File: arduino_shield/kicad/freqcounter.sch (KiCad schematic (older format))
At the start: 29 parts, among them J1 ICSP PICKIT, J10 INPUT_A, J11 INPUT_B, J12 INPUT_ZCD, J13 I2C_1, J14 I2C_2, J15 PARALEL, J2 Arduino_Power, J3 Arduino_Power, J4 Arduino_Digital_2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

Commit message: Arduino Shield PCB designed
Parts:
- removed J5: Digital_2, Footprints:Connector_1x06, symbol Connector:Conn_01x06_Female
- removed J6: Analog, Footprints:Connector_1x04, symbol Connector:Conn_01x04_Female
- removed J8: Digital_1, Footprints:Connector_1x06, symbol Connector:Conn_01x06_Female
- added J5: Digital_2, Footprints:Connector_1x08, symbol Connector:Conn_01x08_Female
- added J6: Analog, Footprints:Connector_1x06, symbol Connector:Conn_01x06_Female
- added J8: Digital_1, Footprints:Connector_1x08, symbol Connector:Conn_01x08_Female
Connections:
- net VDD is gone; now on net 5V: J1.2 (Pin_2), J13.3 (Pin_3), J14.3 (Pin_3), J15.1 (Pin_1), R5.1, R6.1
- net ARD_RX: now also U1.11 (RB6), J8.8 (Pin_8); no longer U1.15 (RC1)
- net ARD_TX: now also J8.7 (Pin_7)
- net GND: now also J5.2 (Pin_2)
- net P0: now also U1.13 (RB4); no longer U1.9 (RC7)
- net P1: now also U1.14 (RC2); no longer U1.10 (RB7)
- net P2: now also U1.15 (RC1); no longer U1.11 (RB6)
- net P3: now also U1.16 (RC0); no longer U1.12 (RB5)
- net SCL: now also U1.10 (RB7), J6.6 (Pin_6); no longer U1.13 (RB4)
- net SDA: now also U1.9 (RC7), J6.5 (Pin_5); no longer U1.14 (RC2)
- net at J4.1 (Pin_1): now also J5.1 (Pin_1)
- net at J4.3 (Pin_3): now also J5.3 (Pin_3)
- net at J4.4 (Pin_4): now also J5.4 (Pin_4)
- net at J4.5 (Pin_5): now also J5.5 (Pin_5)
- net at J4.6 (Pin_6): now also J5.6 (Pin_6)
- net at J4.7 (Pin_7): now also J5.7 (Pin_7)
- net at J4.8 (Pin_8): now also J5.8 (Pin_8)
- net at J9.1 (Pin_1): now also J8.1 (Pin_1)
- net at J9.2 (Pin_2): now also J8.2 (Pin_2)
- net at J9.3 (Pin_3): now also J8.3 (Pin_3)
- net at J9.4 (Pin_4): now also J8.4 (Pin_4)
- net at J9.5 (Pin_5): now also J8.5 (Pin_5)
- net at J9.6 (Pin_6): now also J8.6 (Pin_6)
- net at J7.1 (Pin_1): now also J6.1 (Pin_1)
- net at J7.2 (Pin_2): now also J6.2 (Pin_2)
- net at J7.3 (Pin_3): now also J6.3 (Pin_3)
- net at J7.4 (Pin_4): now also J6.4 (Pin_4)
- net at R2.2: now also U1.12 (RB5); no longer U1.16 (RC0)
- no-connect marks 2 -> 1
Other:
- moved on the sheet: R2
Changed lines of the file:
@@
 MCLR
 Text GLabel 6700 1000 0    40   Input ~ 0
-VDD
+5V
 Text GLabel 6700 1100 0    40   Input ~ 0
 GND
@@
 P 2900 1500
 F 0 "J4" H 2800 1500 50  0000 C CNN
-F 1 "Arduino_Digital_2" H 3000 1950 50  0000 C CNN
+F 1 "Arduino_Digital_2" H 2800 1950 50  0000 C CNN
 F 2 "Footprints:Connector_1x08" H 2900 1500 50  0001 C CNN
 F 3 "~" H 2900 1500 50  0001 C CNN
@@
 Text Notes 1200 900  0    100  ~ 0
 ARDUINO INTERFACE
-Text GLabel 1200 2700 2    40   Input ~ 0
+Text GLabel 1400 2900 2    40   Input ~ 0
 SCL
-Text GLabel 1200 2600 2    40   Input ~ 0
+Text GLabel 1400 2800 2    40   Input ~ 0
 SDA
-Text GLabel 2700 2900 0    40   Input ~ 0
+Text GLabel 2500 3100 0    40   Input ~ 0
 ARD_RX
-Text GLabel 2700 2800 0    40   Input ~ 0
+Text GLabel 2500 3000 0    40   Input ~ 0
 ARD_TX
 Text GLabel 1200 1600 2    40   Input ~ 0
@@
 Text GLabel 1200 1300 2    40   Input ~ 0
 3.3V
-Text GLabel 2700 1300 0    40   Input ~ 0
-GND
-Text GLabel 8000 2800 2    40   Input ~ 0
+Text GLabel 8000 3200 2    40   Input ~ 0
 ARD_TX
-Text GLabel 7200 2900 2    40   Input ~ 0
+Text GLabel 7200 3300 2    40   Input ~ 0
 ARD_RX
-Text GLabel 7200 3100 2    40   Input ~ 0
+Text GLabel 6200 3300 0    40   Input ~ 0
 SCL
-Text GLabel 7200 3000 2    40   Input ~ 0
+Text GLabel 6200 3200 0    40   Input ~ 0
 SDA
 $Comp
@@
 L Device:R R2
 U 1 1 5EA58FDB
-P 7650 2800
-F 0 "R2" V 7600 2950 50  0000 L CNN
-F 1 "180" V 7645 2725 50  0000 L CNN
-F 2 "Resistor_SMD:R_0805_2012Metric_Pad1.15x1.40mm_HandSolder" V 7580 2800 50  0001 C CNN
-F 3 "~" H 7650 2800 50  0001 C CNN
-	1    7650 2800
+P 7650 3200
+F 0 "R2" V 7600 3350 50  0000 L CNN
+F 1 "180" V 7645 3125 50  0000 L CNN
+F 2 "Resistor_SMD:R_0805_2012Metric_Pad1.15x1.40mm_HandSolder" V 7580 3200 50  0001 C CNN
+F 3 "~" H 7650 3200 50  0001 C CNN
+	1    7650 3200
 	0    1    1    0
 $EndComp
 Wire Wire Line
-	8000 2800 7800 2800
-Wire Wire Line
-	7500 2800 7200 2800
+	8000 3200 7800 3200
+Wire Wire Line
+	7500 3200 7200 3200
 $Comp
 L Device:C C1
@@
 $EndComp
 Text GLabel 7700 5100 2    40   Input ~ 0
-VDD
+5V
 Wire Wire Line
 	7700 4900 7600 4900
@@
 $EndComp
 Text GLabel 8400 5100 2    40   Input ~ 0
-VDD
+5V
 Wire Wire Line
 	8400 4900 8300 4900
@@
 Text GLabel 8400 5000 2    40   Input ~ 0
 SDA
-Text GLabel 7200 3200 2    40   Input ~ 0
+Text GLabel 7200 2800 2    40   Input ~ 0
 P3
-Text GLabel 7200 3300 2    40   Input ~ 0
+Text GLabel 7200 2900 2    40   Input ~ 0
 P2
-Text GLabel 6200 3200 0    40   Input ~ 0
+Text GLabel 7200 3100 2    40   Input ~ 0
 P0
-Text GLabel 6200 3300 0    40   Input ~ 0
+Text GLabel 7200 3000 2    40   Input ~ 0
 P1
 Text GLabel 9100 5200 2    40   Input ~ 0
@@
 GND
 Text GLabel 9100 4900 2    40   Input ~ 0
-VDD
+5V
 Wire Wire Line
 	9100 4900 9000 4900
@@
 Text GLabel 6100 2400 0    40   Input ~ 0
 5V
-$Comp
-L Connector:Conn_01x06_Female J8
-U 1 1 5EA891A7
-P 2400 2400
-F 0 "J8" H 2500 2400 50  0000 C CNN
-F 1 "Digital_1" H 2350 2750 50  0000 C CNN
-F 2 "Footprints:Connector_1x06" H 2400 2400 50  0001 C CNN
-F 3 "~" H 2400 2400 50  0001 C CNN
-	1    2400 2400
-	-1   0    0    -1
-$EndComp
-$Comp
-L Connector:Conn_01x04_Female J6
-U 1 1 5EA9244B
-P 1500 2300
-F 0 "J6" H 1528 2275 50  0000 L CNN
-F 1 "Analog" H 1350 2550 50  0000 L CNN
-F 2 "Footprints:Connector_1x04" H 1500 2300 50  0001 C CNN
-F 3 "~" H 1500 2300 50  0001 C CNN
-	1    1500 2300
-	1    0    0    -1
-$EndComp
-Wire Wire Line
-	1200 2200 1300 2200
-Wire Wire Line
-	1300 2300 1200 2300
-Wire Wire Line
-	1200 2400 1300 2400
-Wire Wire Line
-	1300 2500 1200 2500
-Wire Wire Line
-	2600 2200 2700 2200
-Wire Wire Line
-	2700 2300 2600 2300
-Wire Wire Line
-	2600 2400 2700 2400
-Wire Wire Line
-	2700 2500 2600 2500
-Wire Wire Line
-	2600 2600 2700 2600
-Wire Wire Line
-	2700 2700 2600 2700
-NoConn ~ 2700 1200
-$Comp
-L Connector:Conn_01x06_Female J5
-U 1 1 5EAA5BE8
-P 2400 1600
-F 0 "J5" H 2500 1400 50  0000 C CNN
-F 1 "Digital_2" V 2500 1700 50  0000 C CNN
-F 2 "Footprints:Connector_1x06" H 2400 1600 50  0001 C CNN
-F 3 "~" H 2400 1600 50  0001 C CNN
-	1    2400 1600
-	-1   0    0    -1
-$EndComp
-Wire Wire Line
-	2600 1400 2700 1400
-Wire Wire Line
-	2700 1500 2600 1500
-Wire Wire Line
-	2600 1600 2700 1600
-Wire Wire Line
-	2700 1700 2600 1700
-Wire Wire Line
-	2600 1800 2700 1800
-Wire Wire Line
-	2700 1900 2600 1900
 Text GLabel 1200 1200 2    40   Input ~ 0
 Reset
@@
 Vin
 Wire Notes Line
-	600  3100 3500 3100
-Wire Notes Line
-	3500 3100 3500 600
-Wire Notes Line
 	3500 600  600  600
-Wire Notes Line
-	600  3100 600  600
 Text GLabel 8800 4100 3    40   Input ~ 0
 SCL
@@
 $EndComp
 Text GLabel 8800 3600 1    40   Input ~ 0
-VDD
+5V
 Wire Wire Line
 	8800 3600 8800 3650
@@
 Wire Wire Line
 	8800 3650 8800 3800
+$Comp
+L Connector:Conn_01x06_Female J6
+U 1 1 5EAB060A
+P 1600 2400
+F 0 "J6" H 1628 2375 50  0000 L CNN
+F 1 "Analog" H 1400 2750 50  0000 L CNN
+F 2 "Footprints:Connector_1x06" H 1600 2400 50  0001 C CNN
+F 3 "~" H 1600 2400 50  0001 C CNN
+	1    1600 2400
+	1    0    0    -1
+$EndComp
+Wire Wire Line
+	1200 2200 1400 2200
+Wire Wire Line
+	1200 2300 1400 2300
+Wire Wire Line
+	1200 2400 1400 2400
+Wire Wire Line
+	1200 2500 1400 2500
+Wire Wire Line
+	1200 2600 1300 2600
+Wire Wire Line
+	1200 2700 1400 2700
+Wire Wire Line
+	1200 2700 1200 2900
+Wire Wire Line
+	1200 2900 1400 2900
+Connection ~ 1200 2700
+Wire Wire Line
+	1400 2800 1300 2800
+Wire Wire Line
+	1300 2800 1300 2600
+Connection ~ 1300 2600
+Wire Wire Line
+	1300 2600 1400 2600
+Wire Wire Line
+	2500 3100 2700 3100
+Wire Wire Line
+	2700 3100 2700 2900
+Wire Wire Line
+	2500 3000 2600 3000
+Wire Wire Line
+	2600 3000 2600 2800
+Wire Wire Line
+	2600 2800 2700 2800
+$Comp
+L Connector:Conn_01x08_Female J8
+U 1 1 5EACC1E4
+P 2300 2500
+F 0 "J8" H 2328 2475 50  0000 L CNN
+F 1 "Digital_1" H 2100 2950 50  0000 L CNN
+F 2 "Footprints:Connector_1x08" H 2300 2500 50  0001 C CNN
+F 3 "~" H 2300 2500 50  0001 C CNN
+	1    2300 2500
+	-1   0    0    -1
+$EndComp
+Wire Wire Line
+	2500 2900 2700 2900
+Connection ~ 2700 2900
+Wire Wire Line
+	2600 2800 2500 2800
+Connection ~ 2600 2800
+Wire Wire Line
+	2500 2700 2700 2700
+Wire Wire Line
+	2500 2600 2700 2600
+Wire Wire Line
+	2500 2500 2700 2500
+Wire Wire Line
+	2500 2400 2700 2400
+Wire Wire Line
+	2500 2300 2700 2300
+Wire Wire Line
+	2500 2200 2700 2200
+Wire Notes Line
+	600  600  600  3300
+Wire Notes Line
+	600  3300 3500 3300
+Wire Notes Line
+	3500 3300 3500 600
+$Comp
+L Connector:Conn_01x08_Female J5
+U 1 1 5EAEC8C6
+P 2300 1500
+F 0 "J5" H 2328 1475 50  0000 L CNN
+F 1 "Digital_2" H 2100 1950 50  0000 L CNN
+F 2 "Footprints:Connector_1x08" H 2300 1500 50  0001 C CNN
+F 3 "~" H 2300 1500 50  0001 C CNN
+	1    2300 1500
+	-1   0    0    -1
+$EndComp
+Wire Wire Line
+	2500 1400 2700 1400
+Wire Wire Line
+	2500 1500 2700 1500
+Wire Wire Line
+	2500 1600 2700 1600
+Wire Wire Line
+	2500 1700 2700 1700
+Wire Wire Line
+	2500 1800 2700 1800
+Wire Wire Line
+	2500 1900 2700 1900
+Wire Wire Line
+	2700 1200 2500 1200
+Wire Wire Line
+	2700 1300 2600 1300
+Text GLabel 2250 1250 0    40   Input ~ 0
+GND
+Wire Wire Line
+	2250 1250 2600 1250
+Wire Wire Line
+	2600 1250 2600 1300
+Connection ~ 2600 1300
+Wire Wire Line
+	2600 1300 2500 1300
 $EndSCHEMATC

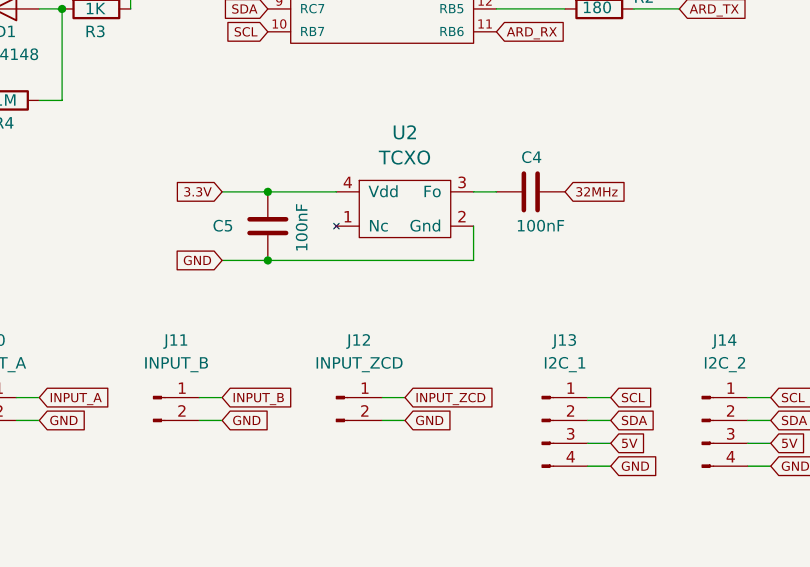
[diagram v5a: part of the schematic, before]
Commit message: Bugfix Arduino-Shield PCB
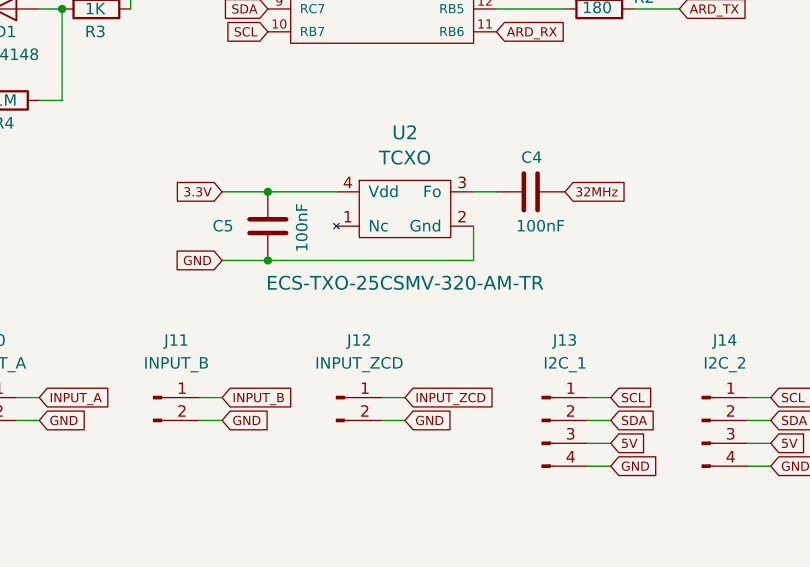
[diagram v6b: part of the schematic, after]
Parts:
- D1: footprint Diode_SMD:D_SOD-123 -> Footprints:SOD-80_HandSolder
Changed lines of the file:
@@
 F 0 "D1" H 5100 3100 50  0000 R CNN
 F 1 "1N4148" H 5200 3000 50  0000 R CNN
-F 2 "Diode_SMD:D_SOD-123" H 5050 3025 50  0001 C CNN
+F 2 "Footprints:SOD-80_HandSolder" H 5050 3025 50  0001 C CNN
 F 3 "https://www.vishay.com/docs/85748/1n4148w.pdf" H 5050 3200 50  0001 C CNN
 	1    5050 3200
@@
 F 1 "TCXO" H 6800 4148 60  0000 C CNN
 F 2 "Footprints:TCXO-5032" H 6700 3950 60  0001 C CNN
-F 3 "" H 6700 3950 60  0000 C CNN
+F 3 "ECS-TXO-25CSMV-320-AM-TR" H 6800 3600 60  0000 C CNN
 	1    6500 4000
 	1    0    0    -1

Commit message: Bugfix Arduino-Shield Schematic and PCB
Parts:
- added R7, R8, R9: 180, Resistor_SMD:R_0805_2012Metric_Pad1.15x1.40mm_HandSolder, symbol Device:R
- R5, R6: value 10K -> 2K2
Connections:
- net Earth is gone; now on net GND: C3.2
- net ARD_RX: now also R7.1; no longer U1.11 (RB6)
- net INPUT_A: now also R8.2; no longer U1.5 (RC5)
- net INPUT_B: now also R9.2; no longer U1.6 (RC4)
- new net: R7.2, U1.11 (RB6)
- new net: R8.1, U1.5 (RC5)
- new net: R9.1, U1.6 (RC4)
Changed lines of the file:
@@
-	0    1    -1   0
-$EndComp
-$Comp
-L power:Earth #PWR01
-U 1 1 5E71FD1E
-P 4400 3200
-F 0 "#PWR01" H 4400 2950 50  0001 C CNN
-F 1 "Earth" H 4400 3050 50  0001 C CNN
-F 2 "" H 4400 3200 50  0001 C CNN
-F 3 "~" H 4400 3200 50  0001 C CNN
-	1    4400 3200
 	0    1    -1   0
 $EndComp
@@
 Text GLabel 6700 1100 0    40   Input ~ 0
 GND
-Text GLabel 6200 2800 0    40   Input ~ 0
+Text GLabel 5500 2800 0    40   Input ~ 0
 INPUT_A
-Text GLabel 6200 2900 0    40   Input ~ 0
+Text GLabel 5500 2900 0    40   Input ~ 0
 INPUT_B
 $Comp
@@
 Text GLabel 8000 3200 2    40   Input ~ 0
 ARD_TX
-Text GLabel 7200 3300 2    40   Input ~ 0
+Text GLabel 8000 3300 2    40   Input ~ 0
 ARD_RX
 Text GLabel 6200 3300 0    40   Input ~ 0
@@
 P 8800 3950
 F 0 "R5" V 8750 4100 50  0000 L CNN
-F 1 "10K" V 8795 3875 50  0000 L CNN
+F 1 "2K2" V 8795 3875 50  0000 L CNN
 F 2 "Resistor_SMD:R_0805_2012Metric_Pad1.15x1.40mm_HandSolder" V 8730 3950 50  0001 C CNN
 F 3 "~" H 8800 3950 50  0001 C CNN
@@
 P 8900 3950
 F 0 "R6" V 8850 4100 50  0000 L CNN
-F 1 "10K" V 8895 3875 50  0000 L CNN
+F 1 "2K2" V 8895 3875 50  0000 L CNN
 F 2 "Resistor_SMD:R_0805_2012Metric_Pad1.15x1.40mm_HandSolder" V 8830 3950 50  0001 C CNN
 F 3 "~" H 8900 3950 50  0001 C CNN
@@
 Wire Wire Line
 	2600 1300 2500 1300
+$Comp
+L Device:R R8
+U 1 1 5EABD611
+P 5650 2800
+F 0 "R8" V 5600 2950 50  0000 L CNN
+F 1 "180" V 5645 2725 50  0000 L CNN
+F 2 "Resistor_SMD:R_0805_2012Metric_Pad1.15x1.40mm_HandSolder" V 5580 2800 50  0001 C CNN
+F 3 "~" H 5650 2800 50  0001 C CNN
+	1    5650 2800
+	0    1    1    0
+$EndComp
+$Comp
+L Device:R R9
+U 1 1 5EABD6A7
+P 5650 2900
+F 0 "R9" V 5600 3050 50  0000 L CNN
+F 1 "180" V 5645 2825 50  0000 L CNN
+F 2 "Resistor_SMD:R_0805_2012Metric_Pad1.15x1.40mm_HandSolder" V 5580 2900 50  0001 C CNN
+F 3 "~" H 5650 2900 50  0001 C CNN
+	1    5650 2900
+	0    1    1    0
+$EndComp
+Wire Wire Line
+	5800 2800 6200 2800
+Wire Wire Line
+	5800 2900 6200 2900
+$Comp
+L Device:R R7
+U 1 1 5EAC87AA
+P 7650 3300
+F 0 "R7" V 7600 3450 50  0000 L CNN
+F 1 "180" V 7645 3225 50  0000 L CNN
+F 2 "Resistor_SMD:R_0805_2012Metric_Pad1.15x1.40mm_HandSolder" V 7580 3300 50  0001 C CNN
+F 3 "~" H 7650 3300 50  0001 C CNN
+	1    7650 3300
+	0    1    1    0
+$EndComp
+Wire Wire Line
+	7800 3300 8000 3300
+Wire Wire Line
+	7500 3300 7200 3300
+Text GLabel 4400 3200 0    40   Input ~ 0
+GND
 $EndSCHEMATC

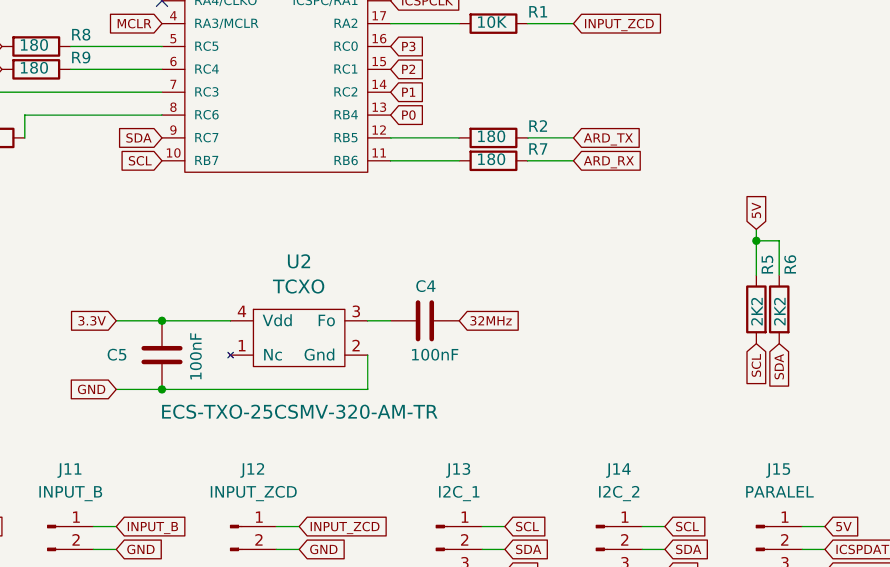
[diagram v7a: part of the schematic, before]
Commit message: Updated Arduino-Shield Schematic and PCB
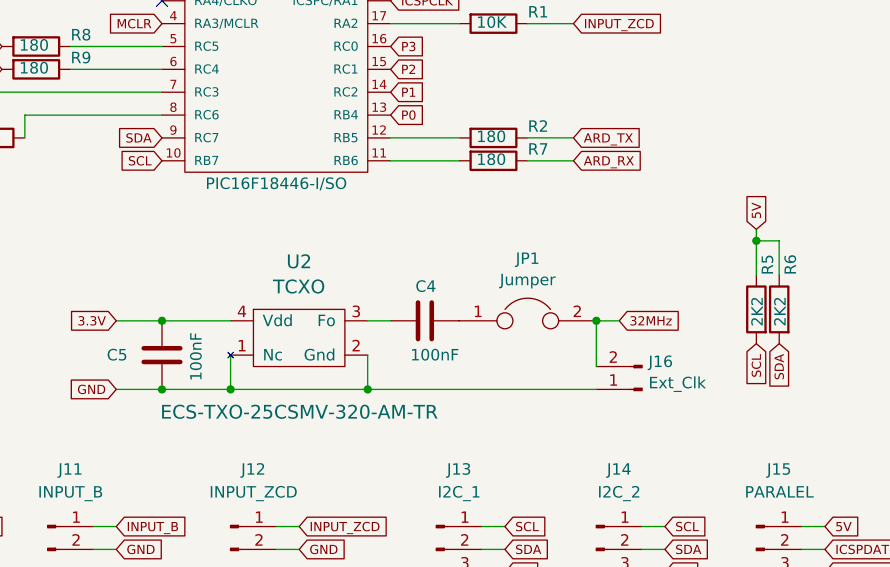
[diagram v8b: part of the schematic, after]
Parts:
- added J16: Ext_Clk, Footprints:PinHeader_1x02, symbol Connector:Conn_01x02_Male
- added JP1: Jumper, Footprints:PinHeader_1x02, symbol Device:Jumper
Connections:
- net 32MHz: now also J16.2 (Pin_2), JP1.2; no longer C4.2
- net GND: now also U2.1 (Nc), J16.1 (Pin_1)
- new net: C4.2, JP1.1
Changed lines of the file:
@@
 F 1 "1N4148" H 5200 3000 50  0000 R CNN
 F 2 "Footprints:SOD-80_HandSolder" H 5050 3025 50  0001 C CNN
-F 3 "https://www.vishay.com/docs/85748/1n4148w.pdf" H 5050 3200 50  0001 C CNN
+F 3 "LS4148-GS18" H 5050 3200 50  0001 C CNN
 	1    5050 3200
 	1    0    0    -1
@@
 F 1 "PIC16F18446" H 6700 2430 50  0000 C CNN
 F 2 "Package_SO:SOIC-20W_7.5x12.8mm_P1.27mm" H 6700 2350 50  0001 C CNN
-F 3 "" H 6700 2350 50  0001 C CNN
+F 3 "PIC16F18446-I/SO" H 6700 1300 50  0000 C CNN
 	1    6700 2350
 	1    0    0    -1
@@
 Connection ~ 6200 4000
 Wire Wire Line
-	6200 4300 7100 4300
+	6200 4300 6500 4300
 Wire Wire Line
 	7100 4300 7100 4150
@@
 	6200 4300 6000 4300
 Connection ~ 6200 4300
-Text GLabel 7500 4000 2    40   Input ~ 0
+Text GLabel 8200 4000 2    40   Input ~ 0
 32MHz
 Wire Wire Line
@@
 Text GLabel 4400 3200 0    40   Input ~ 0
 GND
+$Comp
+L Device:Jumper JP1
+U 1 1 5EAC4D9A
+P 7800 4000
+F 0 "JP1" H 7800 4272 50  0000 C CNN
+F 1 "Jumper" H 7800 4179 50  0000 C CNN
+F 2 "Footprints:PinHeader_1x02" H 7800 4000 50  0001 C CNN
+F 3 "~" H 7800 4000 50  0001 C CNN
+	1    7800 4000
+	1    0    0    -1
+$EndComp
+Wire Wire Line
+	6500 4150 6500 4300
+Connection ~ 6500 4300
+Wire Wire Line
+	6500 4300 7100 4300
+Connection ~ 7100 4300
+$Comp
+L Connector:Conn_01x02_Male J16
+U 1 1 5EAD5B8E
+P 8300 4300
+F 0 "J16" H 8272 4179 50  0000 R CNN
+F 1 "Ext_Clk" H 8272 4272 50  0000 R CNN
+F 2 "Footprints:PinHeader_1x02" H 8300 4300 50  0001 C CNN
+F 3 "~" H 8300 4300 50  0001 C CNN
+	1    8300 4300
+	-1   0    0    1
+$EndComp
+Wire Wire Line
+	8100 4200 8100 4000
+Wire Wire Line
+	7100 4300 8100 4300
+Wire Wire Line
+	8200 4000 8100 4000
+Connection ~ 8100 4000
 $EndSCHEMATC
